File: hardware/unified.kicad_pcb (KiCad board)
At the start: 4 copper layers, 83.7 x 139.7 mm, 143 parts, among them J1 debug-snoop, J303 1x2 jumper right-angle, J304 1x2 jumper right-angle, J305 Conn_02x03_Odd_Even, P1 edge connector, U1 MCP1827S-3302E/EB, U102 74LVC138A, U103 74LVC8T245, U104 74LVC8T245, U105 74LVC8T245, U106 74LVC8T245, U107 74LVC8T245, U108 74LVC8T245, U109 IS66WV51216EBLL, U110 74LVC8T245, U111 74LVC8T245, U112 74LVC8T245, U113 74LVC8T245, U2 74LVC138A, U201 74LVC138A, U202 IS66WV51216EBLL, U203 74LVC8T245, U204 74LVC8T245, U205 74LVC8T245, U206 74LVC8T245, U207 74LVC8T245, U208 74LVC8T245, U209 74LVC8T245, U210 74LVC8T245, U211 74LVC8T245, U212 74LVC8T245, U3 74LVC8T245, U301 74LVC138A, U302 74LVC138A, U303 74LV161A, U304 74LV161A, U305 74LV161A, U306 74LV161A, U307 74LV161A, U308 74LV164A, U309 74LV164A, U310 74AHC74, U311 74LVC2G125, U312 74AHC04, U313 74AHC373, U314 74AHC373, U4 74LVC8T245, U401 74LVC138A, U5 74LVC8T245, U6 S29AL016J55TFIR20, U7 74LVC8T245, U8 74LVC8T245

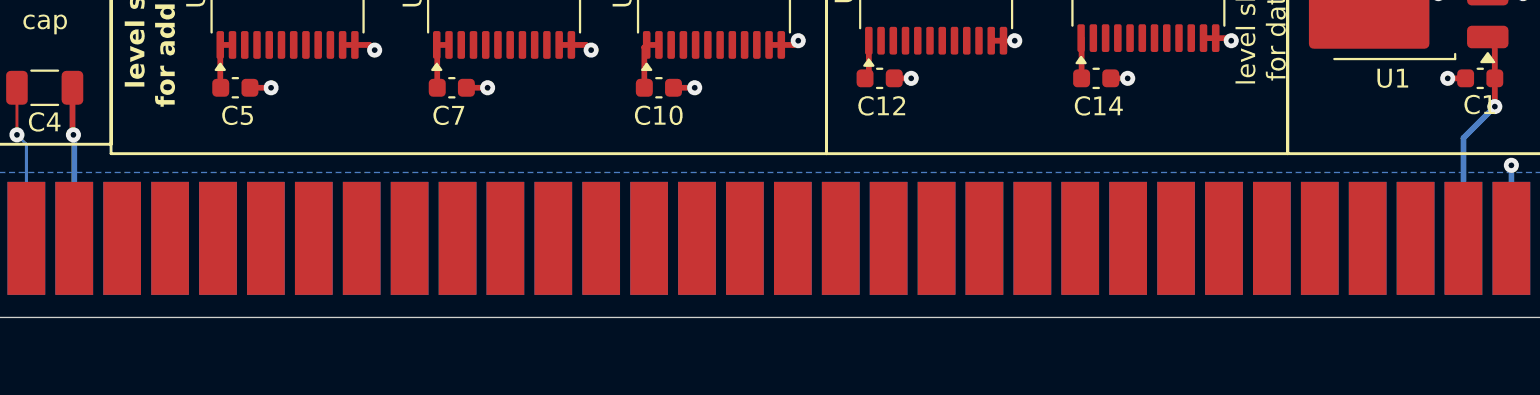
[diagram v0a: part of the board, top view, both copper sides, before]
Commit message: Add manual traces and vias for bottom-side cart teeth
This allows these signals to make it to an inner signal layer during auto-routing.
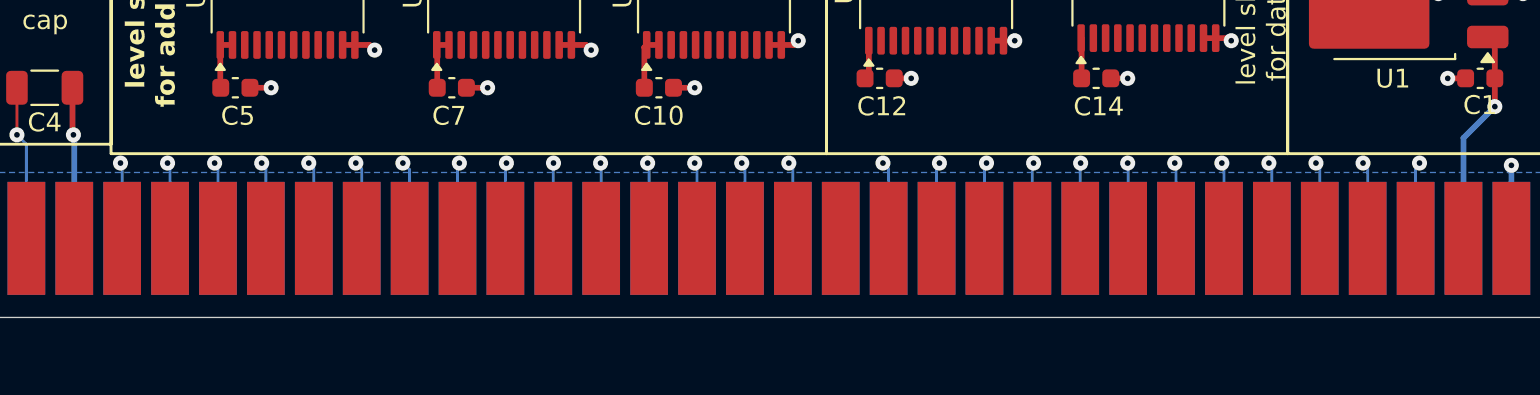
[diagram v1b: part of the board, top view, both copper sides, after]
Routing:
- net SEGA_A5: track 0.00 -> 4.15 mm, vias 0 -> 1
- net SEGA_A13: track 0.00 -> 4.13 mm, vias 0 -> 1
- net SEGA_D7: track 0.00 -> 4.12 mm, vias 0 -> 1
- net SEGA_A6: track 0.00 -> 4.11 mm, vias 0 -> 1
- net SEGA_D3: track 0.00 -> 4.10 mm, vias 0 -> 1
- net SEGA_A12: track 0.00 -> 4.09 mm, vias 0 -> 1
- net SEGA_A1: track 0.00 -> 4.09 mm, vias 0 -> 1
- net SEGA_D11: track 0.00 -> 4.09 mm, vias 0 -> 1
- net SEGA_D4: track 0.00 -> 4.08 mm, vias 0 -> 1
- net SEGA_A7: track 0.00 -> 4.07 mm, vias 0 -> 1
- net SEGA_A17: track 0.00 -> 4.07 mm, vias 0 -> 1
- net SEGA_D10: track 0.00 -> 4.07 mm, vias 0 -> 1
- net SEGA_D0: track 0.00 -> 4.06 mm, vias 0 -> 1
- net SEGA_A11: track 0.00 -> 4.06 mm, vias 0 -> 1
- net SEGA_A2: track 0.00 -> 4.05 mm, vias 0 -> 1
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
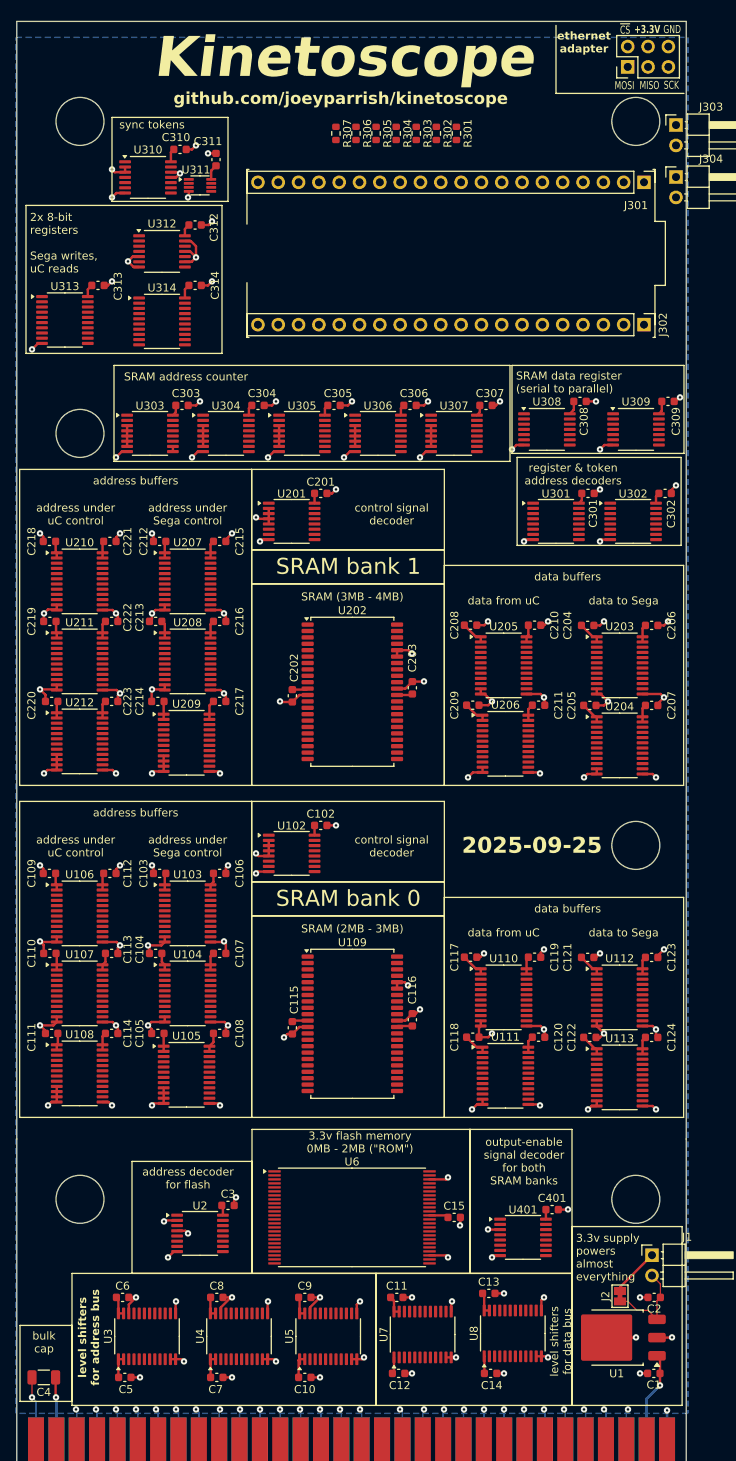
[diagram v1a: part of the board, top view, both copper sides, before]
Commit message: Drop A18 GND connection
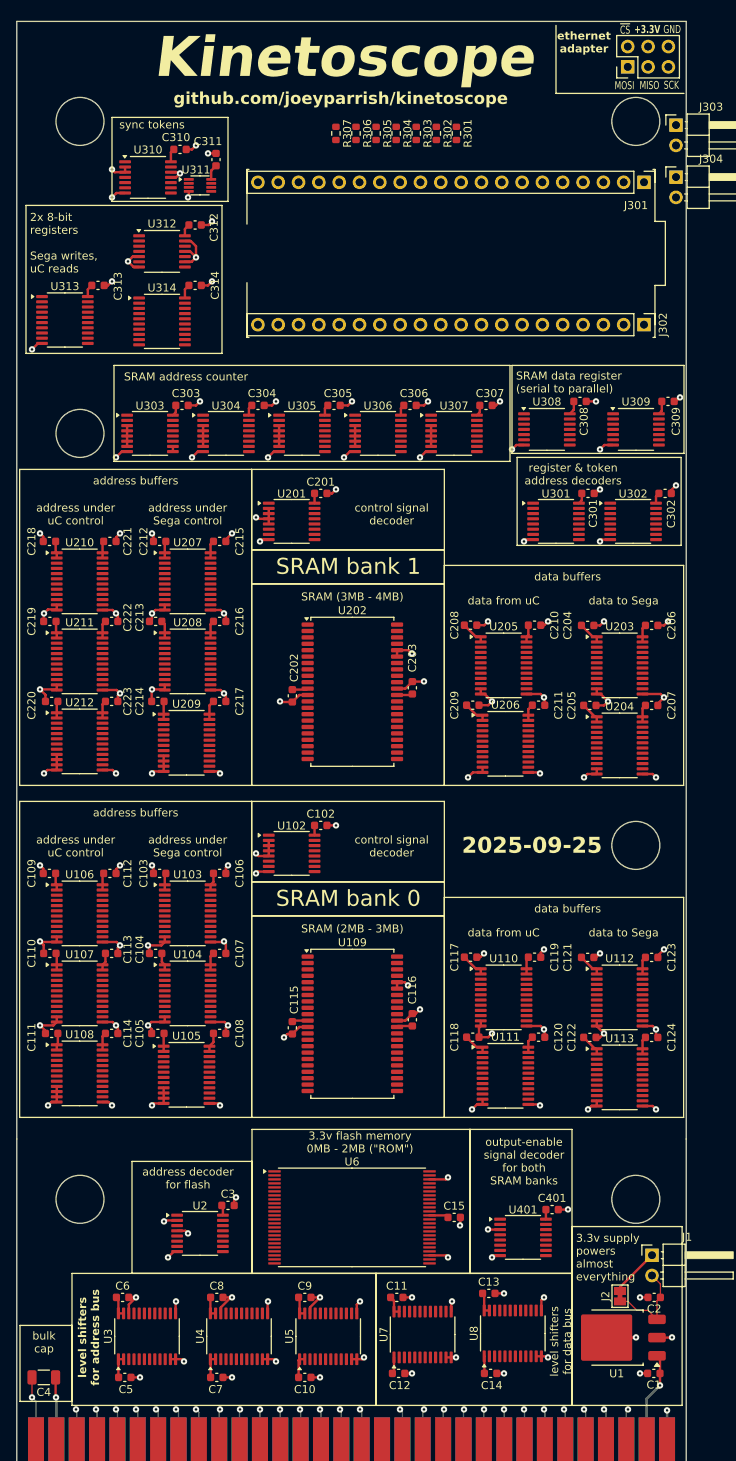
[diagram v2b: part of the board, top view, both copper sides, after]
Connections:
- P1 pad A18: GND -> unconnected-(P1-GND-PadA18)
- U201 pad 1: SRAM_DIS_0 -> SRAM_DIS_1
- U201 pad 10: unconnected-(U102-~{Y5}-Pad10) -> unconnected-(U201-~{Y5}-Pad10)
- U201 pad 11: unconnected-(U102-~{Y4}-Pad11) -> unconnected-(U201-~{Y4}-Pad11)
- U201 pad 12: unconnected-(U102-~{Y3}-Pad12) -> unconnected-(U201-~{Y3}-Pad12)
- U201 pad 13: unconnected-(U102-~{Y2}-Pad13) -> unconnected-(U201-~{Y2}-Pad13)
- U201 pad 14: /sram-bank-internal/~{UC_CONTROL} -> /sram-bank-internal1/~{UC_CONTROL}
- U201 pad 15: /sram-bank-internal/~{SEGA_CONTROL} -> /sram-bank-internal1/~{SEGA_CONTROL}
- U201 pad 7: unconnected-(U102-~{Y7}-Pad7) -> unconnected-(U201-~{Y7}-Pad7)
- U201 pad 9: unconnected-(U102-~{Y6}-Pad9) -> unconnected-(U201-~{Y6}-Pad9)
- U202 pad 1: /sram-bank-internal/SRAM_A4 -> /sram-bank-internal1/SRAM_A4
- U202 pad 10: /sram-bank-internal/SRAM_DATA3 -> /sram-bank-internal1/SRAM_DATA3
- U202 pad 13: /sram-bank-internal/SRAM_DATA4 -> /sram-bank-internal1/SRAM_DATA4
- U202 pad 14: /sram-bank-internal/SRAM_DATA5 -> /sram-bank-internal1/SRAM_DATA5
- U202 pad 15: /sram-bank-internal/SRAM_DATA6 -> /sram-bank-internal1/SRAM_DATA6
- U202 pad 16: /sram-bank-internal/SRAM_DATA7 -> /sram-bank-internal1/SRAM_DATA7
- U202 pad 17: /sram-bank-internal/~{SRAM_FINAL_WE} -> /sram-bank-internal1/~{SRAM_FINAL_WE}
- U202 pad 18: /sram-bank-internal/SRAM_A16 -> /sram-bank-internal1/SRAM_A16
- U202 pad 19: /sram-bank-internal/SRAM_A15 -> /sram-bank-internal1/SRAM_A15
- U202 pad 2: /sram-bank-internal/SRAM_A3 -> /sram-bank-internal1/SRAM_A3
- U202 pad 20: /sram-bank-internal/SRAM_A14 -> /sram-bank-internal1/SRAM_A14
- U202 pad 21: /sram-bank-internal/SRAM_A13 -> /sram-bank-internal1/SRAM_A13
- U202 pad 22: /sram-bank-internal/SRAM_A12 -> /sram-bank-internal1/SRAM_A12
- U202 pad 23: /sram-bank-internal/SRAM_A17 -> /sram-bank-internal1/SRAM_A17
- U202 pad 24: /sram-bank-internal/SRAM_A11 -> /sram-bank-internal1/SRAM_A11
- U202 pad 25: /sram-bank-internal/SRAM_A10 -> /sram-bank-internal1/SRAM_A10
- U202 pad 26: /sram-bank-internal/SRAM_A9 -> /sram-bank-internal1/SRAM_A9
- U202 pad 27: /sram-bank-internal/SRAM_A8 -> /sram-bank-internal1/SRAM_A8
- U202 pad 28: /sram-bank-internal/SRAM_A18 -> /sram-bank-internal1/SRAM_A18
- U202 pad 29: /sram-bank-internal/SRAM_DATA8 -> /sram-bank-internal1/SRAM_DATA8
- U202 pad 3: /sram-bank-internal/SRAM_A2 -> /sram-bank-internal1/SRAM_A2
- U202 pad 30: /sram-bank-internal/SRAM_DATA9 -> /sram-bank-internal1/SRAM_DATA9
- U202 pad 31: /sram-bank-internal/SRAM_DATA10 -> /sram-bank-internal1/SRAM_DATA10
- U202 pad 32: /sram-bank-internal/SRAM_DATA11 -> /sram-bank-internal1/SRAM_DATA11
- U202 pad 35: /sram-bank-internal/SRAM_DATA12 -> /sram-bank-internal1/SRAM_DATA12
- U202 pad 36: /sram-bank-internal/SRAM_DATA13 -> /sram-bank-internal1/SRAM_DATA13
- U202 pad 37: /sram-bank-internal/SRAM_DATA14 -> /sram-bank-internal1/SRAM_DATA14
- U202 pad 38: /sram-bank-internal/SRAM_DATA15 -> /sram-bank-internal1/SRAM_DATA15
- U202 pad 4: /sram-bank-internal/SRAM_A1 -> /sram-bank-internal1/SRAM_A1
- U202 pad 41: /sram-bank-internal/~{SRAM_FINAL_OE} -> /sram-bank-internal1/~{SRAM_FINAL_OE}
- U202 pad 42: /sram-bank-internal/SRAM_A7 -> /sram-bank-internal1/SRAM_A7
- U202 pad 43: /sram-bank-internal/SRAM_A6 -> /sram-bank-internal1/SRAM_A6
- U202 pad 44: /sram-bank-internal/SRAM_A5 -> /sram-bank-internal1/SRAM_A5
- U202 pad 5: /sram-bank-internal/SRAM_A0 -> /sram-bank-internal1/SRAM_A0
- U202 pad 6: /sram-bank-internal/~{SRAM_FINAL_CE} -> /sram-bank-internal1/~{SRAM_FINAL_CE}
- U202 pad 7: /sram-bank-internal/SRAM_DATA0 -> /sram-bank-internal1/SRAM_DATA0
- U202 pad 8: /sram-bank-internal/SRAM_DATA1 -> /sram-bank-internal1/SRAM_DATA1
- U202 pad 9: /sram-bank-internal/SRAM_DATA2 -> /sram-bank-internal1/SRAM_DATA2
- U203 pad 10: /sram-bank-internal/SRAM_DATA7 -> /sram-bank-internal1/SRAM_DATA7
- U203 pad 22: /sram-bank-internal/~{SRAM_FINAL_OE} -> /sram-bank-internal1/~{SRAM_FINAL_OE}
- U203 pad 3: /sram-bank-internal/SRAM_DATA0 -> /sram-bank-internal1/SRAM_DATA0
- U203 pad 4: /sram-bank-internal/SRAM_DATA1 -> /sram-bank-internal1/SRAM_DATA1
- U203 pad 5: /sram-bank-internal/SRAM_DATA2 -> /sram-bank-internal1/SRAM_DATA2
- U203 pad 6: /sram-bank-internal/SRAM_DATA3 -> /sram-bank-internal1/SRAM_DATA3
- U203 pad 7: /sram-bank-internal/SRAM_DATA4 -> /sram-bank-internal1/SRAM_DATA4
- U203 pad 8: /sram-bank-internal/SRAM_DATA5 -> /sram-bank-internal1/SRAM_DATA5
- U203 pad 9: /sram-bank-internal/SRAM_DATA6 -> /sram-bank-internal1/SRAM_DATA6
- U204 pad 10: /sram-bank-internal/SRAM_DATA15 -> /sram-bank-internal1/SRAM_DATA15
- U204 pad 22: /sram-bank-internal/~{SRAM_FINAL_OE} -> /sram-bank-internal1/~{SRAM_FINAL_OE}
- U204 pad 3: /sram-bank-internal/SRAM_DATA8 -> /sram-bank-internal1/SRAM_DATA8
- U204 pad 4: /sram-bank-internal/SRAM_DATA9 -> /sram-bank-internal1/SRAM_DATA9
- U204 pad 5: /sram-bank-internal/SRAM_DATA10 -> /sram-bank-internal1/SRAM_DATA10
- U204 pad 6: /sram-bank-internal/SRAM_DATA11 -> /sram-bank-internal1/SRAM_DATA11
- U204 pad 7: /sram-bank-internal/SRAM_DATA12 -> /sram-bank-internal1/SRAM_DATA12
- U204 pad 8: /sram-bank-internal/SRAM_DATA13 -> /sram-bank-internal1/SRAM_DATA13
- U204 pad 9: /sram-bank-internal/SRAM_DATA14 -> /sram-bank-internal1/SRAM_DATA14
- U205 pad 14: /sram-bank-internal/SRAM_DATA7 -> /sram-bank-internal1/SRAM_DATA7
- U205 pad 15: /sram-bank-internal/SRAM_DATA6 -> /sram-bank-internal1/SRAM_DATA6
- U205 pad 16: /sram-bank-internal/SRAM_DATA5 -> /sram-bank-internal1/SRAM_DATA5
- U205 pad 17: /sram-bank-internal/SRAM_DATA4 -> /sram-bank-internal1/SRAM_DATA4
- U205 pad 18: /sram-bank-internal/SRAM_DATA3 -> /sram-bank-internal1/SRAM_DATA3
- U205 pad 19: /sram-bank-internal/SRAM_DATA2 -> /sram-bank-internal1/SRAM_DATA2
- U205 pad 20: /sram-bank-internal/SRAM_DATA1 -> /sram-bank-internal1/SRAM_DATA1
- U205 pad 21: /sram-bank-internal/SRAM_DATA0 -> /sram-bank-internal1/SRAM_DATA0
- U205 pad 22: /sram-bank-internal/~{UC_CONTROL} -> /sram-bank-internal1/~{UC_CONTROL}
- U206 pad 14: /sram-bank-internal/SRAM_DATA15 -> /sram-bank-internal1/SRAM_DATA15
- U206 pad 15: /sram-bank-internal/SRAM_DATA14 -> /sram-bank-internal1/SRAM_DATA14
- U206 pad 16: /sram-bank-internal/SRAM_DATA13 -> /sram-bank-internal1/SRAM_DATA13
- U206 pad 17: /sram-bank-internal/SRAM_DATA12 -> /sram-bank-internal1/SRAM_DATA12
- U206 pad 18: /sram-bank-internal/SRAM_DATA11 -> /sram-bank-internal1/SRAM_DATA11
- U206 pad 19: /sram-bank-internal/SRAM_DATA10 -> /sram-bank-internal1/SRAM_DATA10
- U206 pad 20: /sram-bank-internal/SRAM_DATA9 -> /sram-bank-internal1/SRAM_DATA9
- U206 pad 21: /sram-bank-internal/SRAM_DATA8 -> /sram-bank-internal1/SRAM_DATA8
- U206 pad 22: /sram-bank-internal/~{UC_CONTROL} -> /sram-bank-internal1/~{UC_CONTROL}
- U207 pad 14: /sram-bank-internal/SRAM_A7 -> /sram-bank-internal1/SRAM_A7
- U207 pad 15: /sram-bank-internal/SRAM_A6 -> /sram-bank-internal1/SRAM_A6
- U207 pad 16: /sram-bank-internal/SRAM_A5 -> /sram-bank-internal1/SRAM_A5
- U207 pad 17: /sram-bank-internal/SRAM_A4 -> /sram-bank-internal1/SRAM_A4
- U207 pad 18: /sram-bank-internal/SRAM_A3 -> /sram-bank-internal1/SRAM_A3
- U207 pad 19: /sram-bank-internal/SRAM_A2 -> /sram-bank-internal1/SRAM_A2
- U207 pad 20: /sram-bank-internal/SRAM_A1 -> /sram-bank-internal1/SRAM_A1
- U207 pad 21: /sram-bank-internal/SRAM_A0 -> /sram-bank-internal1/SRAM_A0
- U207 pad 22: /sram-bank-internal/~{SEGA_CONTROL} -> /sram-bank-internal1/~{SEGA_CONTROL}
- U208 pad 14: /sram-bank-internal/SRAM_A15 -> /sram-bank-internal1/SRAM_A15
- U208 pad 15: /sram-bank-internal/SRAM_A14 -> /sram-bank-internal1/SRAM_A14
- U208 pad 16: /sram-bank-internal/SRAM_A13 -> /sram-bank-internal1/SRAM_A13
- U208 pad 17: /sram-bank-internal/SRAM_A12 -> /sram-bank-internal1/SRAM_A12
- U208 pad 18: /sram-bank-internal/SRAM_A11 -> /sram-bank-internal1/SRAM_A11
- U208 pad 19: /sram-bank-internal/SRAM_A10 -> /sram-bank-internal1/SRAM_A10
- U208 pad 20: /sram-bank-internal/SRAM_A9 -> /sram-bank-internal1/SRAM_A9
- U208 pad 21: /sram-bank-internal/SRAM_A8 -> /sram-bank-internal1/SRAM_A8
- U208 pad 22: /sram-bank-internal/~{SEGA_CONTROL} -> /sram-bank-internal1/~{SEGA_CONTROL}
- U209 pad 14: unconnected-(U105-B8-Pad14) -> unconnected-(U209-B8-Pad14)
- U209 pad 15: unconnected-(U105-B7-Pad15) -> unconnected-(U209-B7-Pad15)
- U209 pad 16: /sram-bank-internal/~{SRAM_FINAL_WE} -> /sram-bank-internal1/~{SRAM_FINAL_WE}
- U209 pad 17: /sram-bank-internal/~{SRAM_FINAL_CE} -> /sram-bank-internal1/~{SRAM_FINAL_CE}
- U209 pad 18: /sram-bank-internal/~{SRAM_FINAL_OE} -> /sram-bank-internal1/~{SRAM_FINAL_OE}
- U209 pad 19: /sram-bank-internal/SRAM_A18 -> /sram-bank-internal1/SRAM_A18
- U209 pad 20: /sram-bank-internal/SRAM_A17 -> /sram-bank-internal1/SRAM_A17
- U209 pad 21: /sram-bank-internal/SRAM_A16 -> /sram-bank-internal1/SRAM_A16
- U209 pad 22: /sram-bank-internal/~{SEGA_CONTROL} -> /sram-bank-internal1/~{SEGA_CONTROL}
- U209 pad 6: /sram-bank-internal/~{SRAM_OE} -> /sram-bank-internal1/~{SRAM_OE}
- U210 pad 14: /sram-bank-internal/SRAM_A7 -> /sram-bank-internal1/SRAM_A7
- U210 pad 15: /sram-bank-internal/SRAM_A6 -> /sram-bank-internal1/SRAM_A6
- U210 pad 16: /sram-bank-internal/SRAM_A5 -> /sram-bank-internal1/SRAM_A5
- U210 pad 17: /sram-bank-internal/SRAM_A4 -> /sram-bank-internal1/SRAM_A4
- U210 pad 18: /sram-bank-internal/SRAM_A3 -> /sram-bank-internal1/SRAM_A3
- U210 pad 19: /sram-bank-internal/SRAM_A2 -> /sram-bank-internal1/SRAM_A2
- U210 pad 20: /sram-bank-internal/SRAM_A1 -> /sram-bank-internal1/SRAM_A1
- U210 pad 21: /sram-bank-internal/SRAM_A0 -> /sram-bank-internal1/SRAM_A0
- U210 pad 22: /sram-bank-internal/~{UC_CONTROL} -> /sram-bank-internal1/~{UC_CONTROL}
- U211 pad 14: /sram-bank-internal/SRAM_A15 -> /sram-bank-internal1/SRAM_A15
- U211 pad 15: /sram-bank-internal/SRAM_A14 -> /sram-bank-internal1/SRAM_A14
- U211 pad 16: /sram-bank-internal/SRAM_A13 -> /sram-bank-internal1/SRAM_A13
- U211 pad 17: /sram-bank-internal/SRAM_A12 -> /sram-bank-internal1/SRAM_A12
- U211 pad 18: /sram-bank-internal/SRAM_A11 -> /sram-bank-internal1/SRAM_A11
- U211 pad 19: /sram-bank-internal/SRAM_A10 -> /sram-bank-internal1/SRAM_A10
- U211 pad 20: /sram-bank-internal/SRAM_A9 -> /sram-bank-internal1/SRAM_A9
- U211 pad 21: /sram-bank-internal/SRAM_A8 -> /sram-bank-internal1/SRAM_A8
- U211 pad 22: /sram-bank-internal/~{UC_CONTROL} -> /sram-bank-internal1/~{UC_CONTROL}
- U212 pad 14: unconnected-(U108-B8-Pad14) -> unconnected-(U212-B8-Pad14)
- U212 pad 15: unconnected-(U108-B7-Pad15) -> unconnected-(U212-B7-Pad15)
- U212 pad 16: /sram-bank-internal/~{SRAM_FINAL_WE} -> /sram-bank-internal1/~{SRAM_FINAL_WE}
- U212 pad 17: /sram-bank-internal/~{SRAM_FINAL_CE} -> /sram-bank-internal1/~{SRAM_FINAL_CE}
- U212 pad 18: /sram-bank-internal/~{SRAM_FINAL_OE} -> /sram-bank-internal1/~{SRAM_FINAL_OE}
- U212 pad 19: /sram-bank-internal/SRAM_A18 -> /sram-bank-internal1/SRAM_A18
- U212 pad 20: /sram-bank-internal/SRAM_A17 -> /sram-bank-internal1/SRAM_A17
- U212 pad 21: /sram-bank-internal/SRAM_A16 -> /sram-bank-internal1/SRAM_A16
- U212 pad 22: /sram-bank-internal/~{UC_CONTROL} -> /sram-bank-internal1/~{UC_CONTROL}
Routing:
- net unconnected-(P1-GND-PadA18): track 0.00 -> 1.05 mm
- net GND: track 289.4 -> 288.4 mm
- removed copper zone on B.Cu, net GND

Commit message: Expand unified board by a LOT
Hoping that this makes routing easier.
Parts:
- removed the P4 at (23.0, 64.0)
- added P3: , , F.Cu at (23.0, 145.5)
- added P5: , , F.Cu at (23.0, 65.5)
- added P6: , , F.Cu at (92.5, 65.5)
- added P7: , , F.Cu at (23.0, -4.50)
- added P8: , , F.Cu at (92.5, -4.50)
- moved C301 115.6 mm to (30.2, -29.5)
- moved C302 115.6 mm to (39.9, -29.5)
- moved U301 115.6 mm to (26.2, -26.0)
- moved U302 115.6 mm to (35.9, -26.0)
- moved J301 94.5 mm to (93.5, -61.9)
- moved J302 94.5 mm to (93.5, -44.1)
- moved J305 94.5 mm to (91.5, -76.3)
- moved P10 94.5 mm to (92.5, -72.0)
- moved P9 94.5 mm to (23.0, -72.0)
- moved X301 94.5 mm to (93.5, -61.9)
- moved C312 81.9 mm to (78.1, -33.0)
- moved C313 81.9 mm to (66.0, -25.5)
- moved C314 81.9 mm to (78.1, -25.5)
- moved U312 81.9 mm to (74.0, -29.8)
- moved U313 81.9 mm to (61.9, -21.2)
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- renumbered P6 to P10, P3 to P4, P5 to P9
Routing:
- net GND: track 288.4 -> 269.1 mm, vias 133 -> 149
- net SEGA_A5: track 4.15 -> 0.00 mm, vias 1 -> 0
- net SEGA_A13: track 4.13 -> 0.00 mm, vias 1 -> 0
- net SEGA_D7: track 4.12 -> 0.00 mm, vias 1 -> 0
- net SEGA_A6: track 4.11 -> 0.00 mm, vias 1 -> 0
- net SEGA_D3: track 4.10 -> 0.00 mm, vias 1 -> 0
- net SEGA_A12: track 4.09 -> 0.00 mm, vias 1 -> 0
- net SEGA_A1: track 4.09 -> 0.00 mm, vias 1 -> 0
- net SEGA_D11: track 4.09 -> 0.00 mm, vias 1 -> 0
- net SEGA_D4: track 4.08 -> 0.00 mm, vias 1 -> 0
- net SEGA_A7: track 4.07 -> 0.00 mm, vias 1 -> 0
- net SEGA_A17: track 4.07 -> 0.00 mm, vias 1 -> 0
- net SEGA_D10: track 4.07 -> 0.00 mm, vias 1 -> 0
- net SEGA_D0: track 4.06 -> 0.00 mm, vias 1 -> 0
- net SEGA_A11: track 4.06 -> 0.00 mm, vias 1 -> 0
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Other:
- board size 83.7 x 139.7 mm -> 83.7 x 264.2 mm
- board text added: "SRAM address counter - always written sequentially"
- board text removed: "SRAM address counter"

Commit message: Rearrange unified board layout again
Trying to make routing work better
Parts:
- removed P3, P4, P5, P6, P7, P8: , 
- moved C307 84.7 mm to (26.0, 77.8), turned to -90 degrees
- moved U307 78.1 mm to (22.5, 73.8), turned to -90 degrees
- moved C309 70.4 mm to (56.0, 63.5), turned to -90 degrees
- moved C306 69.7 mm to (26.0, 66.8), turned to -90 degrees
- moved J304 69.3 mm to (27.0, -60.0), turned to 180 degrees
- moved U309 64.0 mm to (52.5, 59.5), turned to -90 degrees
- moved J303 63.5 mm to (27.0, -53.5), turned to 180 degrees
- moved U306 62.9 mm to (22.5, 62.8), turned to -90 degrees
- moved C308 55.3 mm to (56.0, 52.5), turned to -90 degrees
- moved C305 54.7 mm to (26.0, 55.4), turned to -90 degrees
- moved U111 48.9 mm to (68.5, 155.1)
- moved C117 48.9 mm to (64.2, 134.0)
- moved C118 48.9 mm to (64.5, 150.2)
- moved C119 48.9 mm to (72.2, 134.0)
- moved C120 48.9 mm to (72.7, 150.2)
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
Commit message: First successful routing of a unified PCB
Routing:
- net GND: track 269.1 -> 1699.5 mm
- net +3.3V: track 169.9 -> 1266.4 mm, vias 0 -> 9
- net SEGA_D0: track 0.00 -> 377.5 mm, vias 0 -> 9
- net +5V: track 20.7 -> 390.1 mm, vias 1 -> 7
- net SEGA_A1: track 0.00 -> 345.7 mm, vias 0 -> 7
- net ~{SEGA_OE}: track 0.00 -> 333.5 mm, vias 0 -> 6
- net SEGA_D2: track 0.00 -> 333.1 mm, vias 0 -> 6
- net ~{SEGA_AS}: track 0.00 -> 332.6 mm, vias 0 -> 5
- net SEGA_D6: track 0.00 -> 330.5 mm, vias 0 -> 6
- net SEGA_D3: track 0.00 -> 318.8 mm, vias 0 -> 6
- net SEGA_D5: track 0.00 -> 318.7 mm, vias 0 -> 6
- net ~{SEGA_WE_LB}: track 0.00 -> 317.0 mm, vias 0 -> 5
- net SEGA_D1: track 0.00 -> 316.8 mm, vias 0 -> 6
- net SEGA_A2: track 0.00 -> 311.8 mm, vias 0 -> 3
- net SEGA_D4: track 0.00 -> 311.3 mm, vias 0 -> 7
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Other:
- board text added: "2025-09-27"
- board text added: "This edge beveled, hard-gold plating on these teeth, both sides"
- board text removed: "2025-09-25"
